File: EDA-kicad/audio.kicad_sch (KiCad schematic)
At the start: 37 parts, among them J4 SJ2-35894B-SMT-TR, U12 IM68A130A, U13 TPA2038D1YFFR, U14 TPA2038D1YFFR, U3 CODEC-TLV320AIC3204IRHBR, U5 IM68A130A

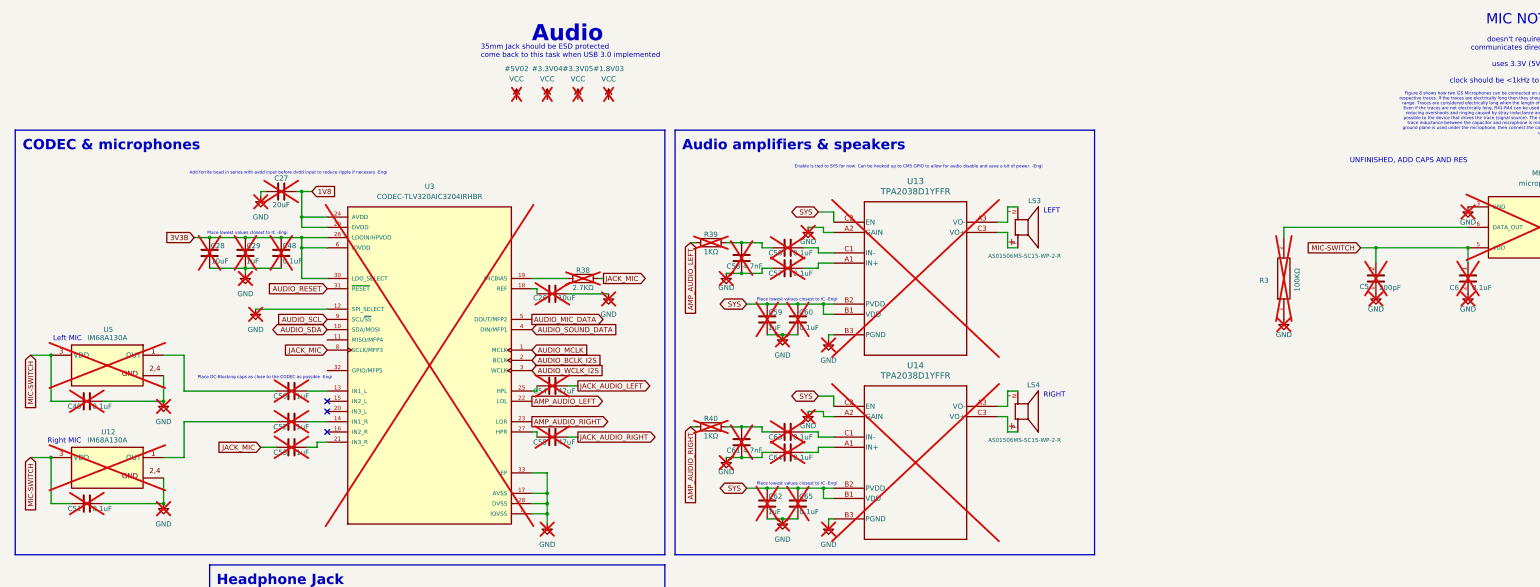
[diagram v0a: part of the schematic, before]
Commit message: reannotate entire schematic
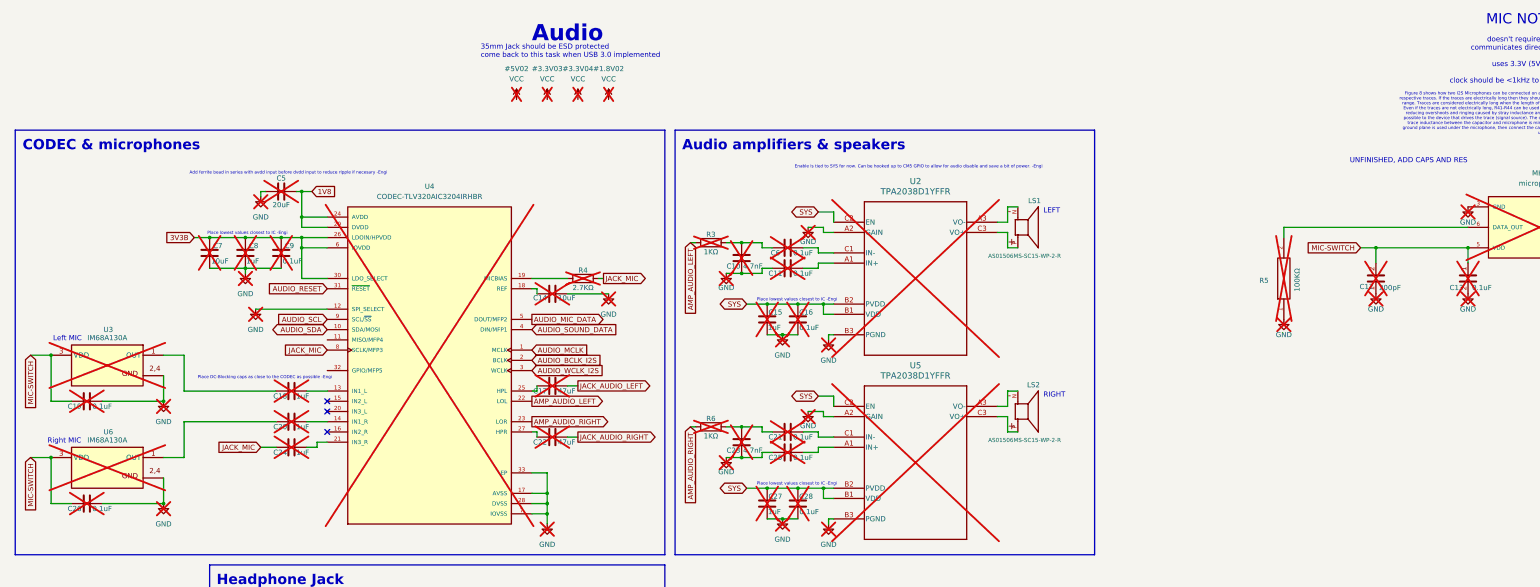
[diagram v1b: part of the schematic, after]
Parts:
- renumbered C58 to C10, C57 to C11, C5 to C12, C6 to C13, C26 to C14, C59 to C15, C60 to C16, C54 to C17, C50 to C18, C49 to C19, C52 to C20, C63 to C21, C55 to C22, C61 to C23, C53 to C24, C64 to C25, C51 to C26, C62 to C27, C65 to C28, C27 to C5, C56 to C6, C28 to C7, C29 to C8, C48 to C9, LS3 to LS1, LS4 to LS2, R39 to R3, R38 to R4, R3 to R5, R40 to R6, U13 to U2, U5 to U3, U3 to U4, U14 to U5, U12 to U6
